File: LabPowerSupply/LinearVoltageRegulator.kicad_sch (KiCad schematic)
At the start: 5 parts

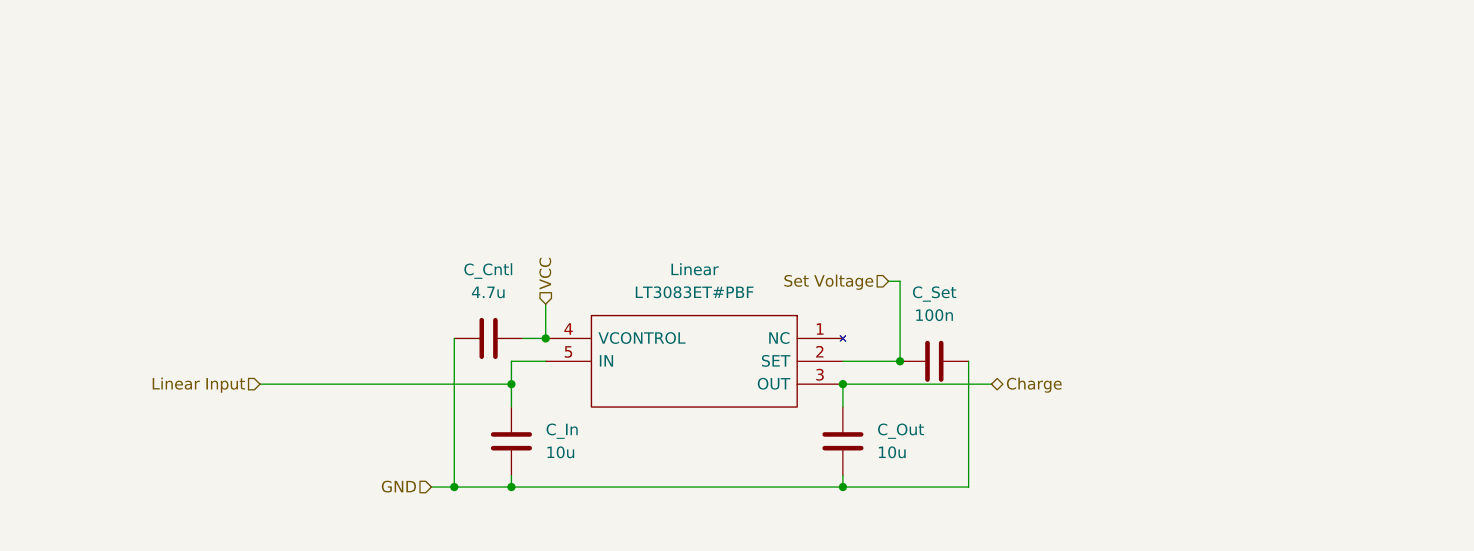
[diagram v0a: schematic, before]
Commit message: Finished first pass on the schematic
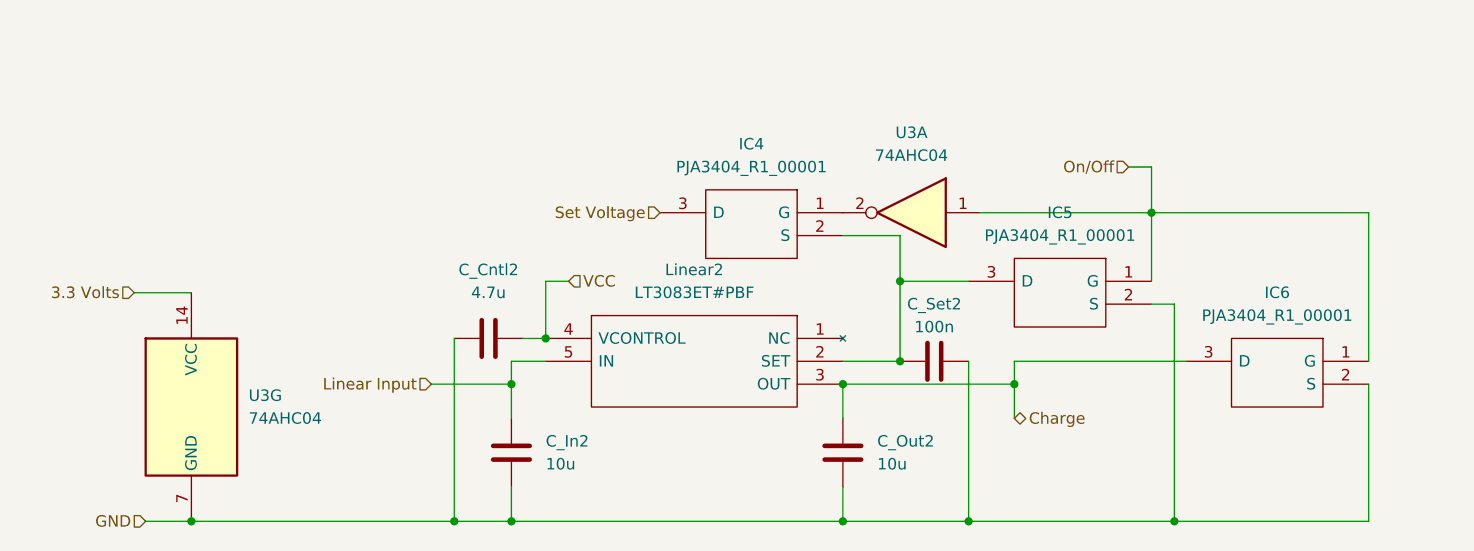
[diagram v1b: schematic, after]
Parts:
- added IC4, IC5, IC6: PJA3404_R1_00001, SamacSys_Parts:SOT95P240X110-3N, symbol SamacSys_Parts:PJA3404_R1_00001
- added U3: 74AHC04, symbol 74xx:74AHC04
- Linear2: renamed from Linear; footprint TO170P457X1022X2306-5P -> SamacSys_Parts:TO170P457X1022X2306-5P
- renumbered C_Cntl to C_Cntl2, C_In to C_In2, C_Out to C_Out2, C_Set to C_Set2
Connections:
- net Charge: now also IC6.3 (D)
- net GND: now also IC5.2 (S), IC6.2 (S), U3.7 (GND)
- net Set Voltage: now also IC4.3 (D); no longer C_Set2.1, Linear2.2 (SET)
- new net: IC4.1 (G), U3.2
- new net: C_Set2.1, IC4.2 (S), IC5.3 (D), Linear2.2 (SET)
- new net 3.3 Volts: U3.14 (VCC)
- new net On/Off: IC5.1 (G), IC6.1 (G), U3.1
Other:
- moved on the sheet: C_In2, C_Out2

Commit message: started PCB
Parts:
- U3: footprint (none) -> Package_DIP:DIP-14_W7.62mm
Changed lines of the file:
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@@
       (effects (font (size 1.27 1.27)) (justify left))
     )
-    (property "Footprint" "" (id 2) (at 82.55 102.87 0)
+    (property "Footprint" "Package_DIP:DIP-14_W7.62mm" (id 2) (at 82.55 102.87 0)
       (effects (font (size 1.27 1.27)) hide)
     )
@@
     (property "Reference" "U3" (id 0) (at 162.56 72.39 0))
     (property "Value" "74AHC04" (id 1) (at 162.56 74.93 0))
-    (property "Footprint" "" (id 2) (at 162.56 81.28 0)
+    (property "Footprint" "Package_DIP:DIP-14_W7.62mm" (id 2) (at 162.56 81.28 0)
       (effects (font (size 1.27 1.27)) hide)
     )

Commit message: more work
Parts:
- renumbered C_Cntl2 to C1_LVR1, C_In2 to C2_LVR1, C_Out2 to C3_LVR1, C_Set2 to C4_LVR1, U3 to Inverter1, Linear2 to Linear1, IC4 to Q1_LVR1, IC5 to Q2_LVR1, IC6 to Q3_LVR1
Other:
- moved on the sheet: Inverter1A, Q1_LVR1

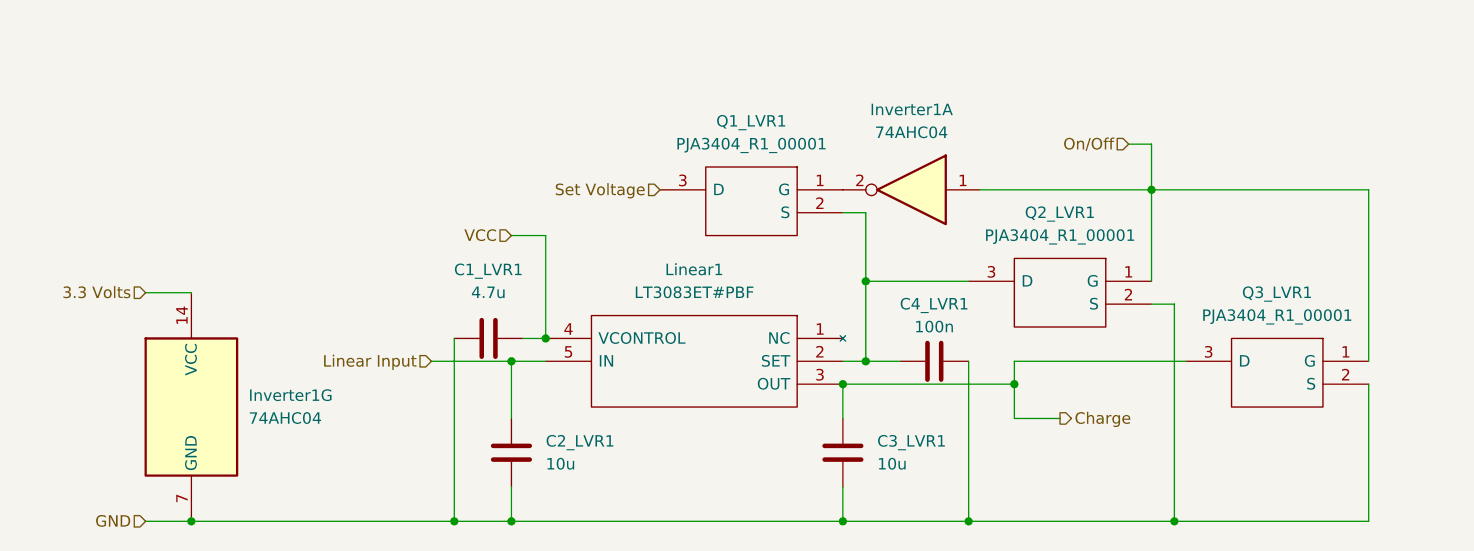
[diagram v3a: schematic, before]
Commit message: Added gate resistors
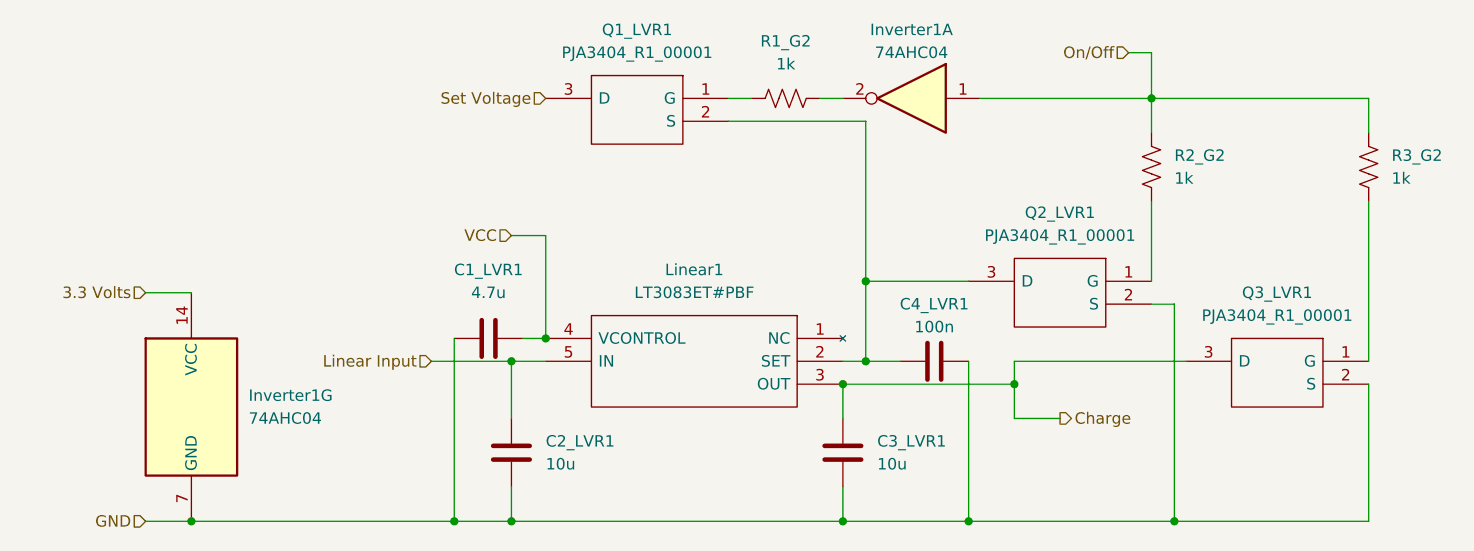
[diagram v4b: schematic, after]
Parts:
- added R1_G2, R2_G2, R3_G2: 1k, Resistor_SMD:R_1210_3225Metric, symbol Device:R_US
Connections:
- net On/Off: now also R2_G2.2, R3_G2.2; no longer Q2_LVR1.1 (G), Q3_LVR1.1 (G)
- net at Inverter1.2: now also R1_G2.2; no longer Q1_LVR1.1 (G)
- new net: Q3_LVR1.1 (G), R3_G2.1
- new net: Q1_LVR1.1 (G), R1_G2.1
- new net: Q2_LVR1.1 (G), R2_G2.1
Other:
- moved on the sheet: Inverter1A, Q1_LVR1

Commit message: Resistor footprints changed to 0603
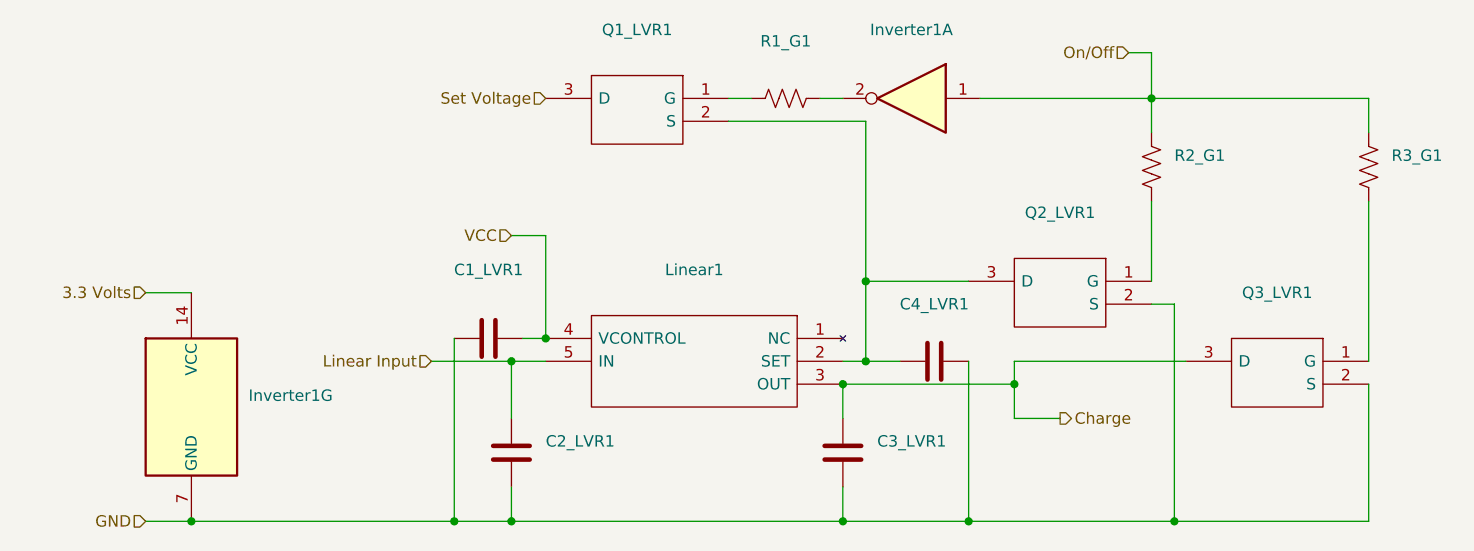
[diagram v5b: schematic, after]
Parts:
- C1_LVR1: value 4.7u -> (none); footprint Capacitor_SMD:C_1210_3225Metric -> (none)
- C2_LVR1, C3_LVR1: value 10u -> (none); footprint Capacitor_SMD:C_1210_3225Metric -> (none)
- C4_LVR1: value 100n -> (none); footprint Capacitor_SMD:C_1210_3225Metric -> (none)
- Inverter1: value 74AHC04 -> (none); footprint Package_DIP:DIP-14_W7.62mm -> (none)
- Linear1: value LT3083ET#PBF -> (none); footprint SamacSys_Parts:TO170P457X1022X2306-5P -> (none)
- Q1_LVR1, Q2_LVR1, Q3_LVR1: value PJA3404_R1_00001 -> (none); footprint SamacSys_Parts:SOT95P240X110-3N -> (none)
- R1_G1: renamed from R1_G2; value 1k -> (none); footprint Resistor_SMD:R_1210_3225Metric -> (none)
- R2_G1: renamed from R2_G2; value 1k -> (none); footprint Resistor_SMD:R_1210_3225Metric -> (none)
- R3_G1: renamed from R3_G2; value 1k -> (none); footprint Resistor_SMD:R_1210_3225Metric -> (none)
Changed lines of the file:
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@@
     (in_bom yes) (on_board yes) (fields_autoplaced)
     (property "Reference" "Q3_LVR1" (id 0) (at 203.2 90.17 0))
-    (property "Value" "PJA3404_R1_00001" (id 1) (at 203.2 92.71 0))
-    (property "Footprint" "SamacSys_Parts:SOT95P240X110-3N" (id 2) (at 196.85 95.25 0)
+    (property "Value" "" (id 1) (at 203.2 92.71 0))
+    (property "Footprint" "" (id 2) (at 196.85 95.25 0)
       (effects (font (size 1.27 1.27)) (justify left) hide)
     )
@@
       (effects (font (size 1.27 1.27)) (justify left))
     )
-    (property "Value" "74AHC04" (id 1) (at 88.9 104.1399 0)
-      (effects (font (size 1.27 1.27)) (justify left))
-    )
-    (property "Footprint" "Package_DIP:DIP-14_W7.62mm" (id 2) (at 82.55 102.87 0)
+    (property "Value" "" (id 1) (at 88.9 104.1399 0)
+      (effects (font (size 1.27 1.27)) (justify left))
+    )
+    (property "Footprint" "" (id 2) (at 82.55 102.87 0)
       (effects (font (size 1.27 1.27)) hide)
     )
@@
     (in_bom yes) (on_board yes)
     (property "Reference" "Inverter1" (id 0) (at 162.56 60.96 0))
-    (property "Value" "74AHC04" (id 1) (at 162.56 63.5 0))
-    (property "Footprint" "Package_DIP:DIP-14_W7.62mm" (id 2) (at 162.56 68.58 0)
+    (property "Value" "" (id 1) (at 162.56 63.5 0))
+    (property "Footprint" "" (id 2) (at 162.56 68.58 0)
       (effects (font (size 1.27 1.27)) hide)
     )
@@
     (in_bom yes) (on_board yes) (fields_autoplaced)
     (property "Reference" "Q1_LVR1" (id 0) (at 132.08 60.96 0))
-    (property "Value" "PJA3404_R1_00001" (id 1) (at 132.08 63.5 0))
-    (property "Footprint" "SamacSys_Parts:SOT95P240X110-3N" (id 2) (at 125.73 66.04 0)
+    (property "Value" "" (id 1) (at 132.08 63.5 0))
+    (property "Footprint" "" (id 2) (at 125.73 66.04 0)
       (effects (font (size 1.27 1.27)) (justify left) hide)
     )
@@
   (symbol (lib_id "Device:R_US") (at 148.59 68.58 90) (unit 1)
     (in_bom yes) (on_board yes) (fields_autoplaced)
-    (property "Reference" "R1_G2" (id 0) (at 148.59 62.23 90))
-    (property "Value" "1k" (id 1) (at 148.59 64.77 90))
-    (property "Footprint" "Resistor_SMD:R_1210_3225Metric" (id 2) (at 148.844 67.564 90)
+    (property "Reference" "R1_G1" (id 0) (at 148.59 62.23 90))
+    (property "Value" "" (id 1) (at 148.59 64.77 90))
+    (property "Footprint" "" (id 2) (at 148.844 67.564 90)
       (effects (font (size 1.27 1.27)) hide)
     )
@@
     (in_bom yes) (on_board yes) (fields_autoplaced)
     (property "Reference" "C1_LVR1" (id 0) (at 115.57 87.63 90))
-    (property "Value" "4.7u" (id 1) (at 115.57 90.17 90))
-    (property "Footprint" "Capacitor_SMD:C_1210_3225Metric" (id 2) (at 119.38 94.2848 0)
+    (property "Value" "" (id 1) (at 115.57 90.17 90))
+    (property "Footprint" "" (id 2) (at 119.38 94.2848 0)
       (effects (font (size 1.27 1.27)) hide)
     )
@@
     (in_bom yes) (on_board yes) (fields_autoplaced)
     (property "Reference" "Q2_LVR1" (id 0) (at 179.07 81.28 0))
-    (property "Value" "PJA3404_R1_00001" (id 1) (at 179.07 83.82 0))
-    (property "Footprint" "SamacSys_Parts:SOT95P240X110-3N" (id 2) (at 172.72 86.36 0)
+    (property "Value" "" (id 1) (at 179.07 83.82 0))
+    (property "Footprint" "" (id 2) (at 172.72 86.36 0)
       (effects (font (size 1.27 1.27)) (justify left) hide)
     )
@@
   (symbol (lib_id "Device:R_US") (at 213.36 76.2 180) (unit 1)
     (in_bom yes) (on_board yes) (fields_autoplaced)
-    (property "Reference" "R3_G2" (id 0) (at 215.9 74.9299 0)
+    (property "Reference" "R3_G1" (id 0) (at 215.9 74.9299 0)
       (effects (font (size 1.27 1.27)) (justify right))
     )
-    (property "Value" "1k" (id 1) (at 215.9 77.4699 0)
+    (property "Value" "" (id 1) (at 215.9 77.4699 0)
       (effects (font (size 1.27 1.27)) (justify right))
     )
-    (property "Footprint" "Resistor_SMD:R_1210_3225Metric" (id 2) (at 212.344 75.946 90)
+    (property "Footprint" "" (id 2) (at 212.344 75.946 90)
       (effects (font (size 1.27 1.27)) hide)
     )
@@
     (in_bom yes) (on_board yes) (fields_autoplaced)
     (property "Reference" "Linear1" (id 0) (at 138.43 87.63 0))
-    (property "Value" "LT3083ET#PBF" (id 1) (at 138.43 90.17 0))
-    (property "Footprint" "SamacSys_Parts:TO170P457X1022X2306-5P" (id 2) (at 125.73 92.71 0)
+    (property "Value" "" (id 1) (at 138.43 90.17 0))
+    (property "Footprint" "" (id 2) (at 125.73 92.71 0)
       (effects (font (size 1.27 1.27)) (justify left) hide)
     )
@@
       (effects (font (size 1.27 1.27)) (justify left))
     )
-    (property "Value" "10u" (id 1) (at 158.75 109.2199 0)
-      (effects (font (size 1.27 1.27)) (justify left))
-    )
-    (property "Footprint" "Capacitor_SMD:C_1210_3225Metric" (id 2) (at 155.9052 111.76 0)
+    (property "Value" "" (id 1) (at 158.75 109.2199 0)
+      (effects (font (size 1.27 1.27)) (justify left))
+    )
+    (property "Footprint" "" (id 2) (at 155.9052 111.76 0)
       (effects (font (size 1.27 1.27)) hide)
     )
@@
   (symbol (lib_id "Device:R_US") (at 189.23 76.2 180) (unit 1)
     (in_bom yes) (on_board yes) (fields_autoplaced)
-    (property "Reference" "R2_G2" (id 0) (at 191.77 74.9299 0)
+    (property "Reference" "R2_G1" (id 0) (at 191.77 74.9299 0)
       (effects (font (size 1.27 1.27)) (justify right))
     )
-    (property "Value" "1k" (id 1) (at 191.77 77.4699 0)
+    (property "Value" "" (id 1) (at 191.77 77.4699 0)
       (effects (font (size 1.27 1.27)) (justify right))
     )
-    (property "Footprint" "Resistor_SMD:R_1210_3225Metric" (id 2) (at 188.214 75.946 90)
+    (property "Footprint" "" (id 2) (at 188.214 75.946 90)
       (effects (font (size 1.27 1.27)) hide)
     )
@@
     (in_bom yes) (on_board yes)
     (property "Reference" "C4_LVR1" (id 0) (at 165.1 91.44 90))
-    (property "Value" "100n" (id 1) (at 165.1 93.98 90))
-    (property "Footprint" "Capacitor_SMD:C_1210_3225Metric" (id 2) (at 168.91 96.8248 0)
+    (property "Value" "" (id 1) (at 165.1 93.98 90))
+    (property "Footprint" "" (id 2) (at 168.91 96.8248 0)
       (effects (font (size 1.27 1.27)) hide)
     )
@@
       (effects (font (size 1.27 1.27)) (justify left))
     )
-    (property "Value" "10u" (id 1) (at 121.92 109.2199 0)
-      (effects (font (size 1.27 1.27)) (justify left))
-    )
-    (property "Footprint" "Capacitor_SMD:C_1210_3225Metric" (id 2) (at 119.0752 111.76 0)
-      (effects (font (size 1.27 1.27)) hide)
-    )
+    (property "Value" "" (id 1) (at 121.92 109.2199 0)
+      (effects (font (size 1.27 1.27)) (justify left))
+    )
+    (property "Footprint" "" (id 2) (at 119.0752 111.76 0)
+      (effects (font (size 1.27 1.27)) hide)
+    )

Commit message: Changed capacitor footprints, added resistor and diode to linear
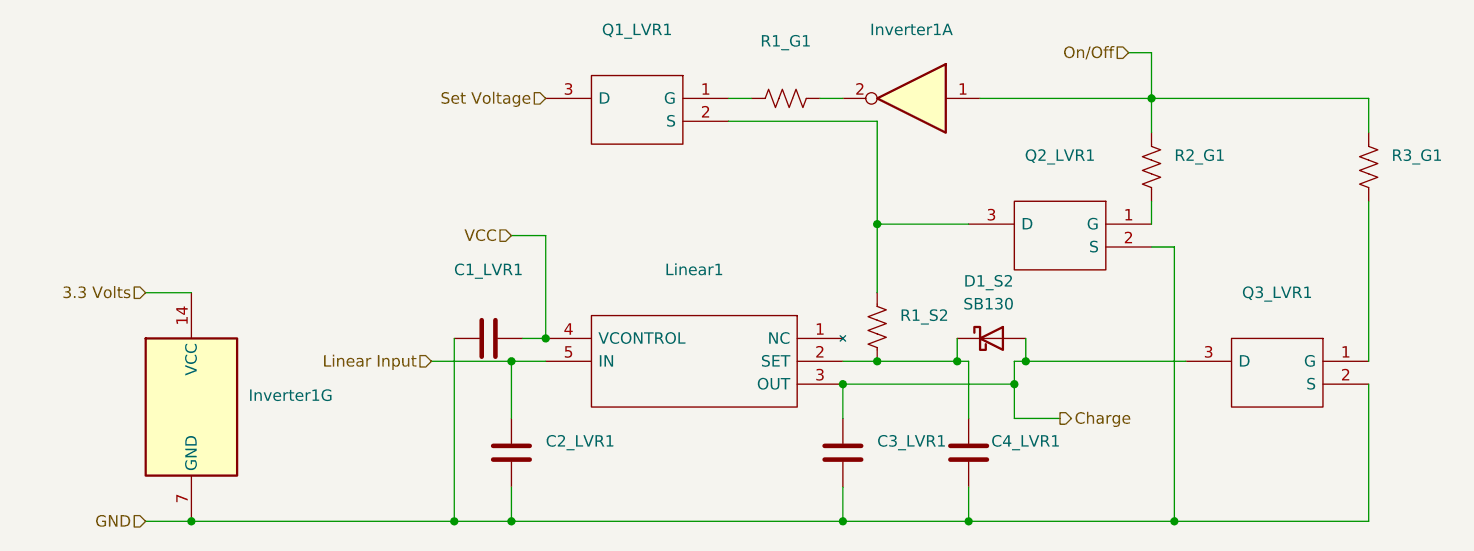
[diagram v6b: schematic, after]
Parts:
- added D1_S2: SB130, Diode_THT:D_DO-41_SOD81_P10.16mm_Horizontal, symbol Diode:SB130
- added R1_S2: (no value), Resistor_SMD:R_0603_1608Metric, symbol Device:R_US
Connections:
- net Charge: now also D1_S2.2 (A)
- net at Q1_LVR1.2 (S), Q2_LVR1.3 (D): now also R1_S2.2; no longer C4_LVR1.1, Linear1.2 (SET)
- new net: C4_LVR1.1, D1_S2.1 (K), Linear1.2 (SET), R1_S2.1
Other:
- moved on the sheet: C4_LVR1, Q2_LVR1
